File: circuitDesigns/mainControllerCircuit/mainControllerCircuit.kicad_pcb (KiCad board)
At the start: 2 copper layers, 128.8 x 128.6 mm, 104 parts, among them J1 USB_A, J13 Moon, J14 LS1-3, J15 SS1-4, J16 SS5-8, J17 SS9-12, J18 LightSensor, J19 OutGND, J2 USB_A, J3 USB_A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

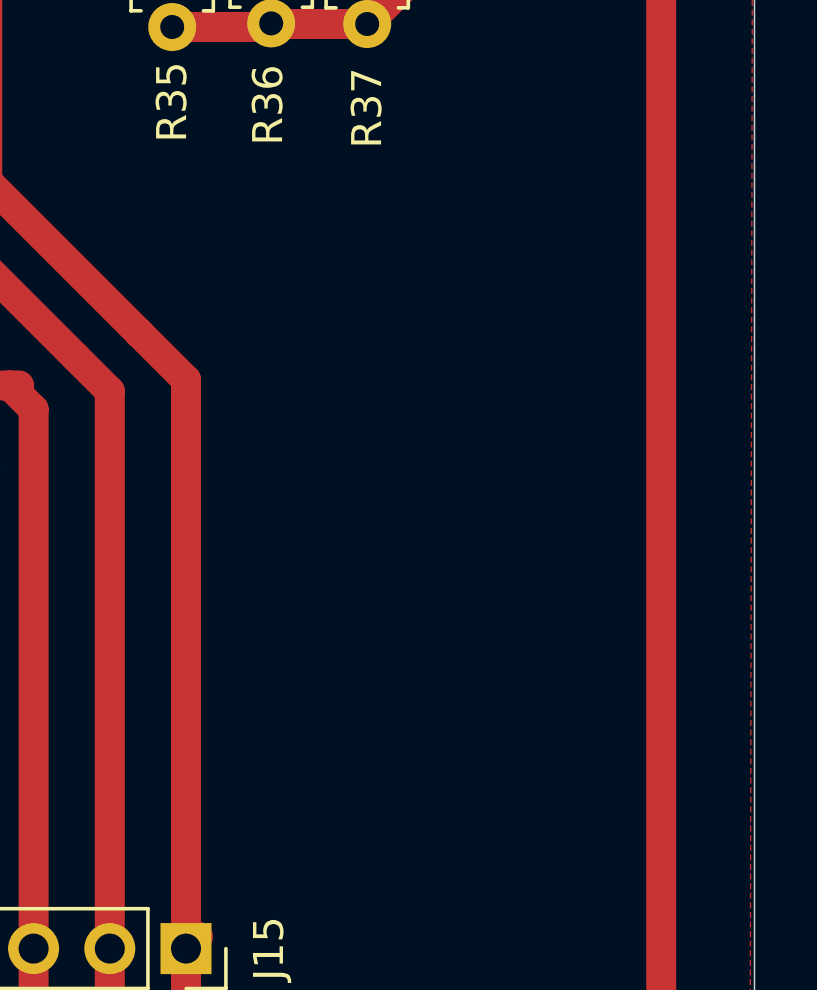
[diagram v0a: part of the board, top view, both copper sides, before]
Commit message: Adds quote to the main controller board
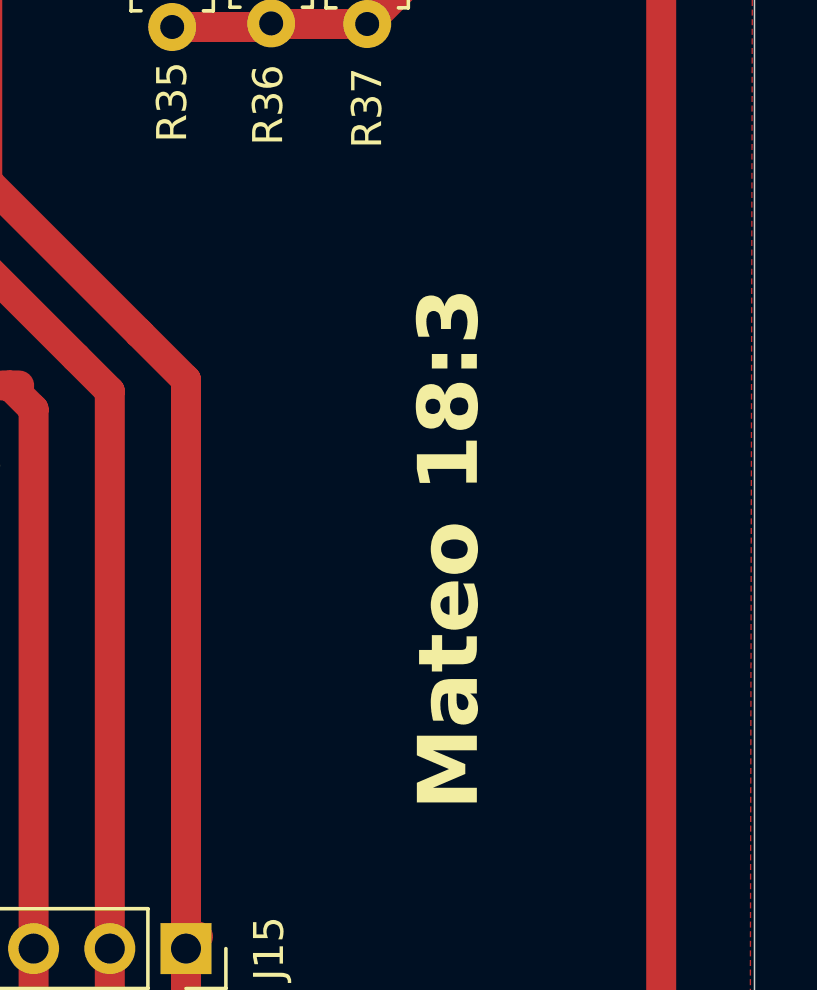
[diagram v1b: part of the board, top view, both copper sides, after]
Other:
- board text added: "Mateo 18:3"
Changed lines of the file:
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@@
 		(layer "Edge.Cuts")
+	)
+	(gr_text "Mateo 18:3"
+		(at 272.6 120.1 90)
+		(layer "F.SilkS")
+		(effects
+			(font
+				(size 2 2)
+				(thickness 0.4)
+				(bold yes)
+			)
+			(justify left bottom)
+		)
 	)
 	(segment
